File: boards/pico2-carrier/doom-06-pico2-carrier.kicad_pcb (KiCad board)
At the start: 2 copper layers, 160 x 62 mm, 35 parts, among them J1 SJ1-3525N, U1 SC1631, U2 PCM5102APWR

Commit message: PCBKit's mark and pcbkit.io on every board; the RP2350 handheld ready to order
The handheld runs from two 18650 cells in parallel behind a DW01A protector and a reverse-cell
P-MOSFET, charged at up to 500 mA from the Pico's USB-C by a BQ24075 (power path into VSYS, timers
off for 6 Ah), with an on/off switch on 3V3_EN, M3 holes, ground pours and the console on pads.
Every assembled part has a JLCPCB code in stock (Basic where there is one); the module sockets are
in the BOM, the modules listed in the order's README. Check complete, the ready review clean.
Every board: routed and checked complete with the new mark.
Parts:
- added logo: , Logo_PCBKit_pcbkit.io, F.Cu at (229.2, 178.0)
- SW1, SW10, SW2, SW3, SW4, SW5, SW6, SW7, SW8, SW9: value (none) -> PTS645SM43SMTR92 LFS

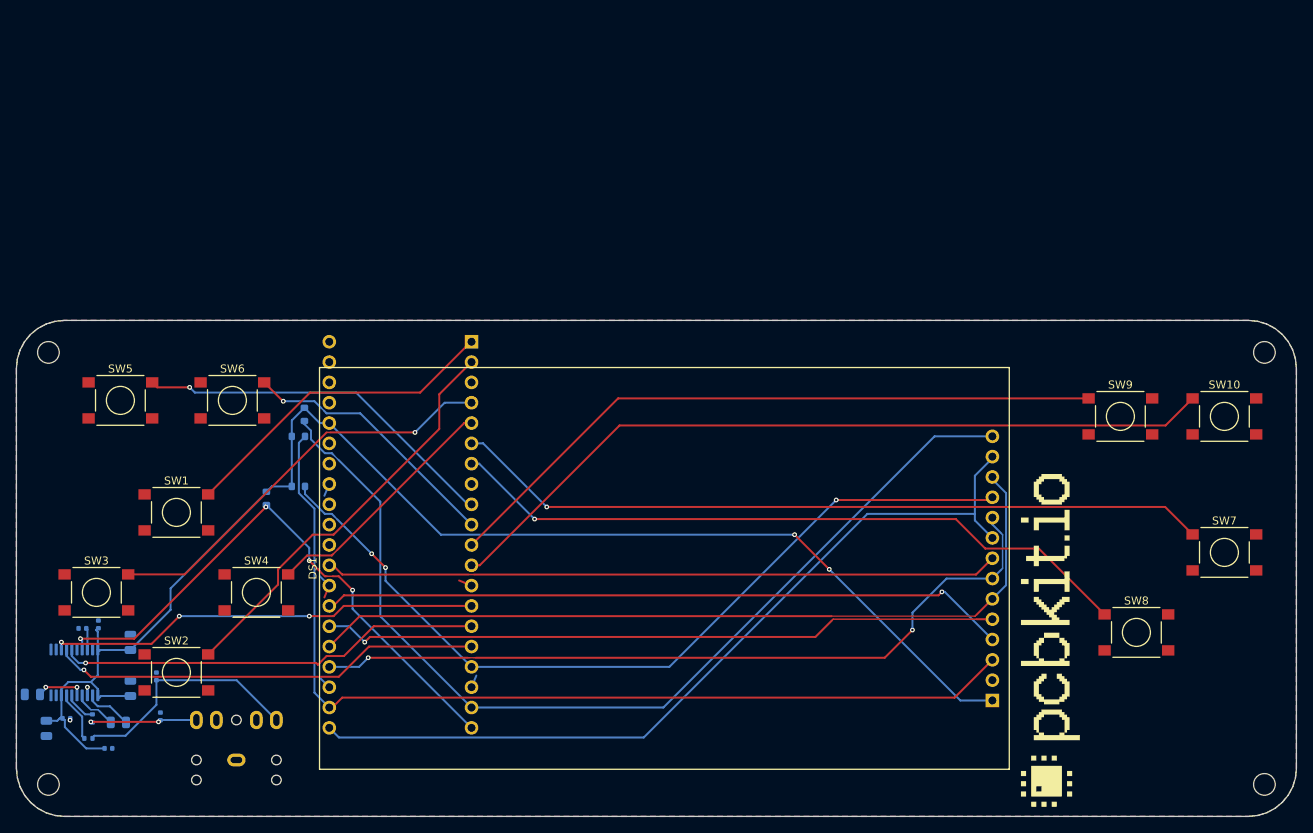
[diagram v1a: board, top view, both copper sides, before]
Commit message: pico2-carrier: two 18650 cells with protection and a USB charger; every part orderable
USB-only power becomes two 18650 in parallel (Keystone 1042 holders on the back) behind a
reverse-cell P-FET and DW01A + FS8205A protection, charged by a BQ24075 with power path from the
module's USB into its VSYS (as boards/rp2350-handheld), an on/off switch on 3V3_EN. Board
160 x 100 mm, M3 holes, test pads, jack on the right edge; the DAC's supplies decoupled at their
pins; every assembled part pinned to an LCSC code; the README says how to charge and flash.
check: complete, 0 errors, 0 warnings; ready lens: nothing to fix; fab export without --force.

Claude-Session: https://claude.ai/code/session_01ATmMmxyrWxFwR3nTdXUrcx
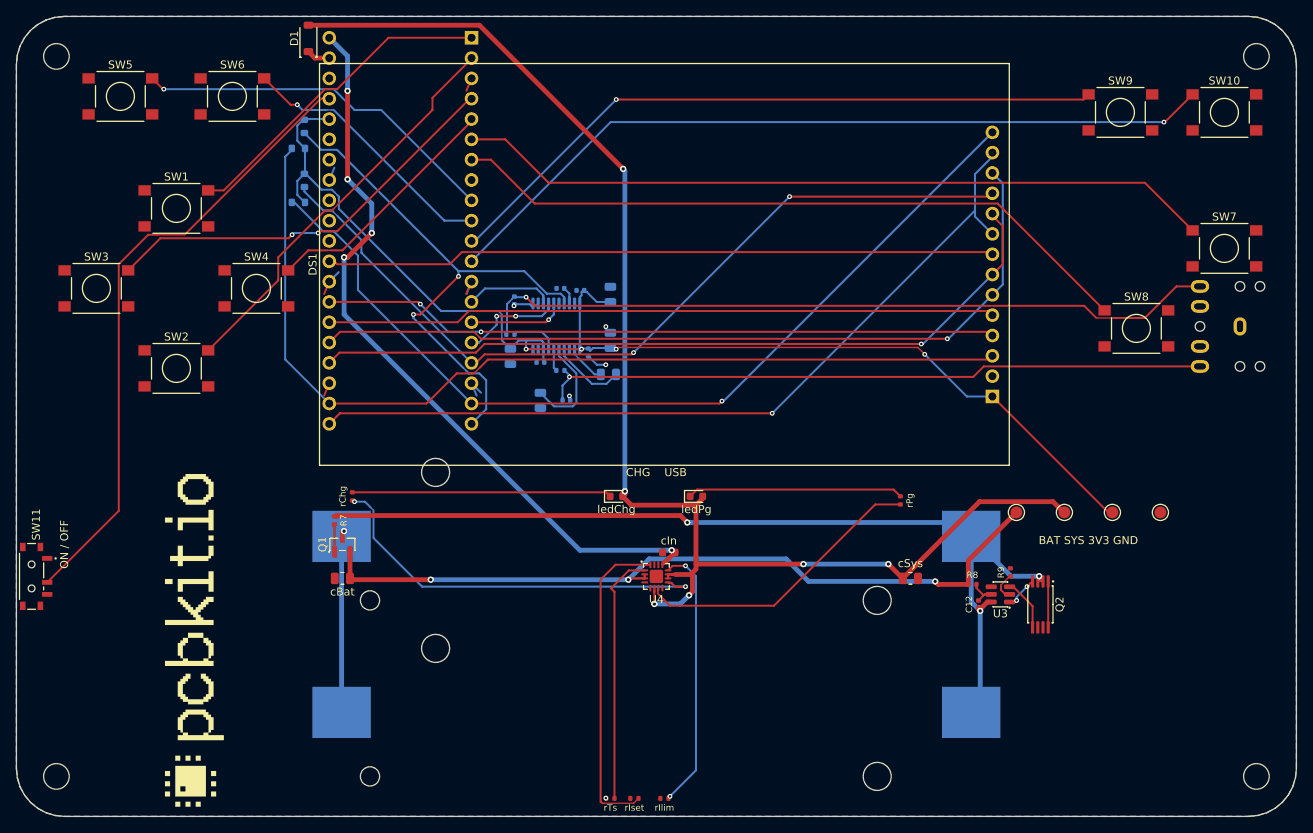
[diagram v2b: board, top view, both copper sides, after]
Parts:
- added BT1: 1042, BatteryHolder_Keystone_1042_1x18650, B.Cu at (180.0, 187.0)
- added BT2: 1042, BatteryHolder_Keystone_1042_1x18650, B.Cu at (180.0, 165.0)
- added C12: 100nF, C_0402_1005Metric, F.Cu at (220.2, 173.5)
- added D1: 1N5819HW-7-F, D_SOD-123, F.Cu at (136.5, 102.8)
- added Q1: AO3401A, SOT-23, F.Cu at (140.8, 166.0)
- added Q2: FS8205A, TSSOP-8_4.4x2.93mm_P0.65mm, F.Cu at (228.0, 173.5)
- added R7: 100kohm, R_0402_1005Metric, F.Cu at (139.8, 163.0)
- added R8: 100ohm, R_0402_1005Metric, F.Cu at (219.5, 171.0)
- added R9: 1kohm, R_0402_1005Metric, F.Cu at (224.2, 169.5)
- added SW11: MSK12C02, SW_Slide_SPDT_Shouhan_MSK12C02, F.Cu at (101.9, 170.0)
- added U3: DW01A, SOT-6_1.6x2.9mm_P0.95mm, F.Cu at (223.0, 172.2)
- added U4: BQ24075RGTR, QFN-16-1EP_3x3mm_P0.5mm_EP1.68x1.68mm, F.Cu at (180.0, 170.0)
- added cBat: 4.7uF, C_0805_2012Metric, F.Cu at (140.8, 170.2)
- added cIn: 1uF, C_0603_1608Metric, F.Cu at (181.6, 167.0)
- added cSys: 4.7uF, C_0805_2012Metric, F.Cu at (211.8, 170.2)
- added ledChg: red, LED_0603_1608Metric, F.Cu at (175.0, 160.0)
- added ledPg: green, LED_0603_1608Metric, F.Cu at (185.0, 160.0)
- added rChg: 1.5kohm, R_0402_1005Metric, F.Cu at (142.0, 160.0)
- added rIlim: 1.18kohm, R_0402_1005Metric, F.Cu at (181.0, 197.8)
- added rIset: 1.13kohm, R_0402_1005Metric, F.Cu at (177.2, 197.8)
- added rPg: 1.5kohm, R_0402_1005Metric, F.Cu at (210.5, 160.5)
- added rTs: 10kohm, R_0402_1005Metric, F.Cu at (174.2, 197.8)
- added tpBat: , TestPoint_Round_D1.5mm, F.Cu at (225.0, 162.0)
- added tpGnd: , TestPoint_Round_D1.5mm, F.Cu at (243.0, 162.0)
- added tpSys: , TestPoint_Round_D1.5mm, F.Cu at (231.0, 162.0)
- added tpV3: , TestPoint_Round_D1.5mm, F.Cu at (237.0, 162.0)
- H1, H2, H3, H4: footprint MountingHole_2.7mm_M2.5 -> MountingHole_3.2mm_M3
- moved J1 141.3 mm to (256.4, 138.8), turned to 270 degrees
- moved logo 107.0 mm to (122.2, 178.0)
- moved C3 77.8 mm to (171.5, 142.0), turned to 90 degrees
- moved C7 75.1 mm to (174.0, 144.8)
- moved C2 74.3 mm to (161.8, 142.5)
- moved U2 74.2 mm to (167.5, 138.8)
- moved C4 74.1 mm to (174.2, 140.5)
- moved C6 74.1 mm to (174.2, 134.8)
- moved C1 74.1 mm to (165.5, 143.2), turned to 0 degrees
- moved C8 73.4 mm to (165.5, 148.0), turned to 90 degrees
- moved C9 73.3 mm to (168.0, 134.0)
- moved C5 73.3 mm to (170.5, 134.2), turned to 0 degrees
- moved R6 73.0 mm to (161.8, 139.8), turned to 0 degrees
- moved R5 72.9 mm to (168.0, 144.2), turned to 180 degrees
- moved C11 64.9 mm to (162.2, 135.5), turned to 90 degrees
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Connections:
- net Net-(C8-1) renamed DAC_VNEG
- net Net-(C9-1) renamed DAC_LDO
- C7 pad 1: Net-(C7-2) -> Net-(C7-1)
- C7 pad 2: Net-(C7-1) -> Net-(C7-2)
- R2 pad 1: V3 -> LCD_CS
- R2 pad 2: LCD_CS -> V3
- R3 pad 1: V3 -> T_IRQ
- R3 pad 2: T_IRQ -> V3
- R4 pad 1: DAC_MUTE -> V3
- R4 pad 2: V3 -> DAC_MUTE
- U1 pad 37: (no net) -> PWR_EN
- U1 pad 39: (no net) -> VSYS
- U1 pad 40: (no net) -> VBUS
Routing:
- net SYS: track 0.00 -> 173.1 mm, vias 0 -> 6
- net CELL_N: track 0.00 -> 117.2 mm, vias 0 -> 3
- net BAT: track 0.00 -> 97.2 mm, vias 0 -> 3
- net VBUS: track 0.00 -> 93.9 mm, vias 0 -> 5
- net PWR_EN: track 0.00 -> 78.4 mm
- net LINE_L: track 13.0 -> 83.8 mm, vias 2 -> 1
- net LINE_R: track 29.9 -> 93.6 mm, vias 0 -> 1
- net CHG_N: track 0.00 -> 50.2 mm, vias 0 -> 2
- net I2S_BCK: track 54.2 -> 11.1 mm, vias 3 -> 0
- net I2S_DIN: track 54.1 -> 12.7 mm, vias 1 -> 2
- net I2S_LRCK: track 53.2 -> 12.1 mm
- net ISET: track 0.00 -> 39.8 mm
- net PG_N: track 0.00 -> 36.9 mm
- net ILIM: track 0.00 -> 33.1 mm, vias 0 -> 2
- net CHG_LED: track 0.00 -> 32.4 mm
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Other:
- board size 160 x 62 mm -> 160 x 100 mm
- board text added: "+"
- board text added: "-"
- board text added: "2 x 18650 Li-ion 3.7 V"
- board text added: "BAT SYS 3V3 GND"
- board text added: "CHG USB"
- board text added: "ON / OFF"
